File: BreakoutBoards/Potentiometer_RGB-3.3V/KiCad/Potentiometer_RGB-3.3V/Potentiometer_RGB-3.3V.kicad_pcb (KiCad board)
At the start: 2 copper layers, 3 parts, among them J1 Conn_01x06_Pin

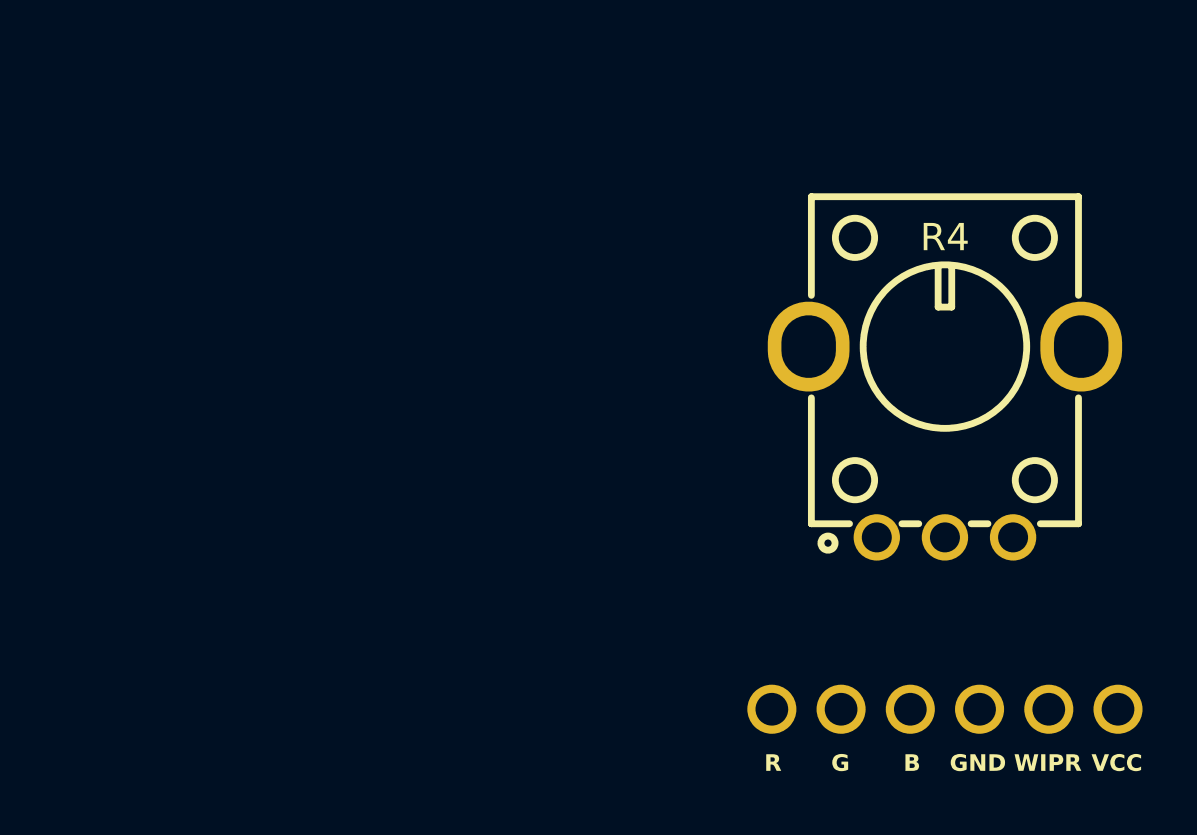
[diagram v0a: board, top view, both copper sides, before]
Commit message: updated to Mk1 and sent for manufacturing
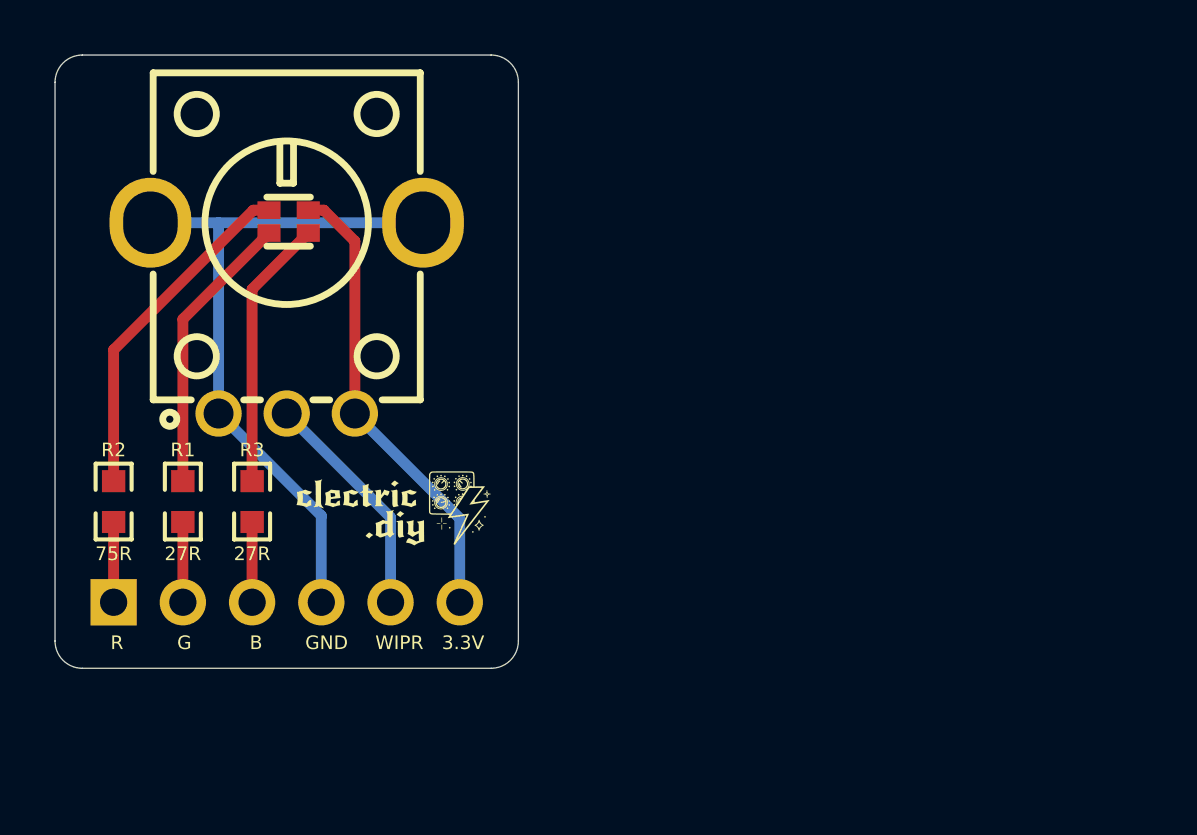
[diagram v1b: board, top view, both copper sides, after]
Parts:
- added G***: LOGO, clectric-diy-branding:clectric.diy-Wordmark-7.5mm, F.Cu at (70.5, 94.2)
- added R1: 27R, clectric-diy:R0603, F.Cu at (62.8, 94.0)
- added R2: 75R, clectric-diy:R0603, F.Cu at (60.2, 94.0)
- added R3: 27R, clectric-diy:R0603, F.Cu at (65.3, 94.0)
- added U2: A-SP1943B1GHR6C-C01-2T, clectric-diy:LED-SMD_4P-L1.6-W1.5-BL_A-SP1943B1GHR6C-C01-2T, F.Cu at (66.7, 83.7)
- J1: footprint clectric-diy:HDR-TH_6P-P2.54-V-M-1 -> Connector_PinHeader_2.54mm:PinHeader_1x06_P2.54mm_Vertical
- moved J1 30.8 mm to (60.2, 97.7), turned to -90 degrees
- moved G*** 24.7 mm to (66.6, 80.6)
- moved R4 24.6 mm to (66.6, 87.2)
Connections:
- net VCC+CW renamed 3.3V+CW
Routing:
- net GND+CCW: track 0.00 -> 25.5 mm
- net 3.3V+CW: track 0.00 -> 17.1 mm
- net LED_RED: track 0.00 -> 15.6 mm
- net LED_GREEN: track 0.00 -> 13.4 mm
- net LED_BLUE: track 0.00 -> 12.9 mm
- net WIPER: track 0.00 -> 8.56 mm
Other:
- board outline added: 17 x 22.5 mm
- board text added: "3.3V"
- board text added: "Charge Potentiometer & 3.3V RGB LED Mk1"
- board text added: "Potentiometer: RK09K1130D62 LED: A-SP1943B1GHR6C-C01-2T"
- board text removed: "Charge Potentiometer_RGB Mk 0.1"
- board text removed: "LED E6C1206RGBC3UDA Potentiometer RK09K1130D62"
- board text removed: "VCC"
